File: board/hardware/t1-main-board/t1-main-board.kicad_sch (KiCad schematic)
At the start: 0 parts

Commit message: Board: capture blk.current-monitors
Five INA236 on I2C1 (0x40-0x43, 0x48) with their shunts, per power tree
§4.12 and BOM v1 lines 54 and 136. The measured branches are rails of
their own (VSYS_SRC, VSYS_LV_AUDIO, VSYS_AUDIO, VSYS_LV_BL, VSYS_P5V1),
fed through the shunts on this sheet; the charger, audio, backlight and
5.1 V sheets take them. The root's layout may leave a stack level empty,
so the block sits under the notes; IC bboxes hold turned rail values;
passive rows hold a bottom rail's text.

Co-Authored-By: Claude Opus 5.5 <noreply@anthropic.com>
Claude-Session: https://claude.ai/code/session_01Ei262h3TpgY9vyfNLMi5Mn
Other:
- added sheet Current monitors (current-monitors.kicad_sch)
- note added: "SoC, memory and the coprocessor; audio, from the DACs to the jacks; instrumentation"
- note removed: "SoC, memory and the coprocessor; audio, from the DACs to the jacks"

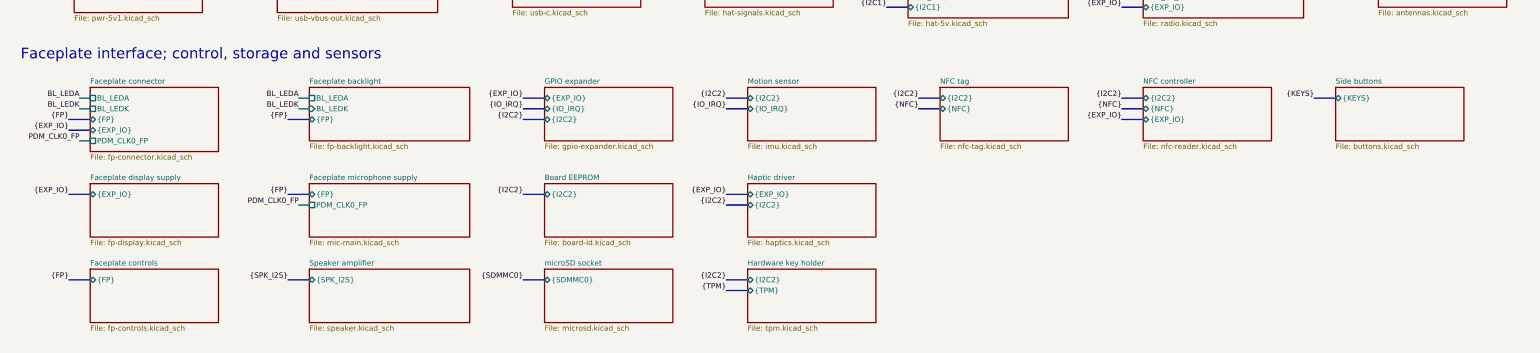
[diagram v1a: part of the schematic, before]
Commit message: Board: capture blk.status-led
LP5521 at 0x32 on I2C2 (BOM v1 line 105) with its charge-pump
capacitors, EN on vcca1v8_pmu, VDD from VSYS_LV through link #22;
LED_R/G/B reach the faceplate connector as the LED bus alias. The
faceplate row of the root is re-packed so five full columns sit left of
the title block.

Co-Authored-By: Claude Opus 5.5 <noreply@anthropic.com>
Claude-Session: https://claude.ai/code/session_01Ei262h3TpgY9vyfNLMi5Mn
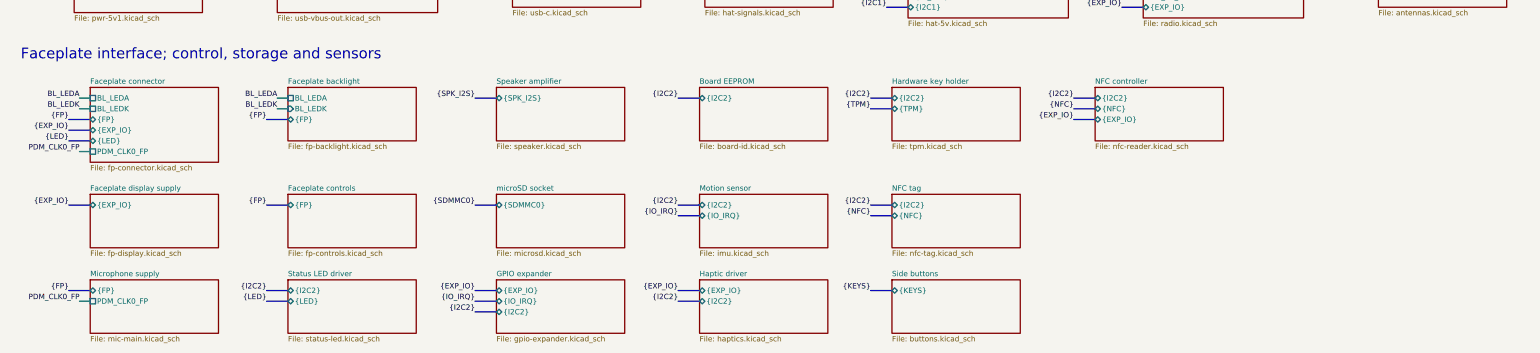
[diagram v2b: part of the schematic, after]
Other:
- sheet Faceplate microphone supply renamed Microphone supply
- added sheet Status LED driver (status-led.kicad_sch)
- sheet Faceplate connector ports: added {LED}; removed none

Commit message: Board: capture blk.debug
Debug UART2 (1.8 V) and I2S/DSD pads with ground pads, reset, PMIC and
power-key pads (PCB-T-09), a pad on every spare SoC GPIO whose pinout v1
row names one (the DEBUG bus, on the SoC's right edge), and a rail pad
for each power-tree rail no other sheet probes (PCB-T-02). Each DAC
sheet carries a pad on its MCLK. The spares pinout v1 leaves without a
pad now carry no-connect flags. On the root, facing sheet pins are
joined directly only where the route meets no other symbol.

Co-Authored-By: Claude Opus 5.5 <noreply@anthropic.com>
Claude-Session: https://claude.ai/code/session_01Ei262h3TpgY9vyfNLMi5Mn
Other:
- added sheet Test and debug access (debug.kicad_sch)
- sheet SoC ports: added {DEBUG}; removed none

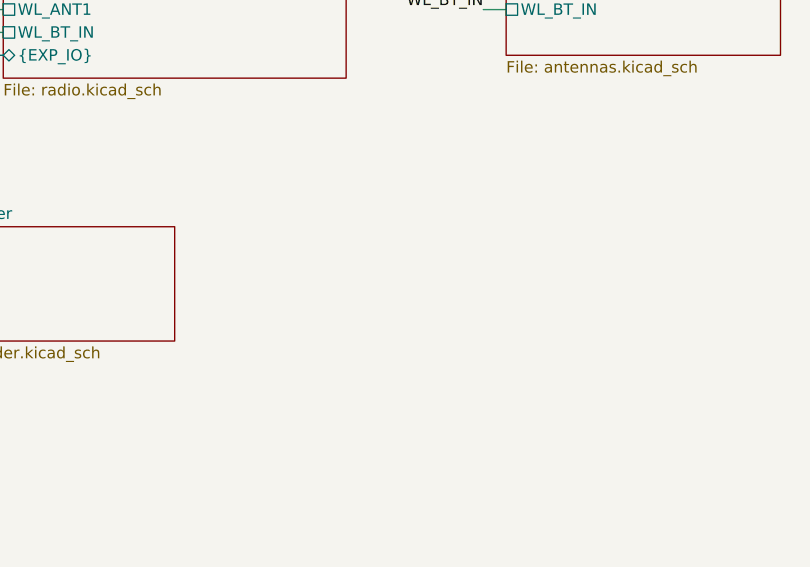
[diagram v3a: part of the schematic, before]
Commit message: Board: capture blk.cover-detect
COVER_DET_N on GPIO0_A6 (AJ38, PMUIO1, wake-capable), recorded in
pinout v1 (closes feature blocks G22): board-edge input and ground pads
for the case's actuator, 100 kΩ to vcc3v3_pmu, TPD1E10B06 at the pad
(BOM v1 line 143, PCB-L-10). The line rides the KEYS bus with the
buttons.

Co-Authored-By: Claude Opus 5.5 <noreply@anthropic.com>
Claude-Session: https://claude.ai/code/session_01Ei262h3TpgY9vyfNLMi5Mn
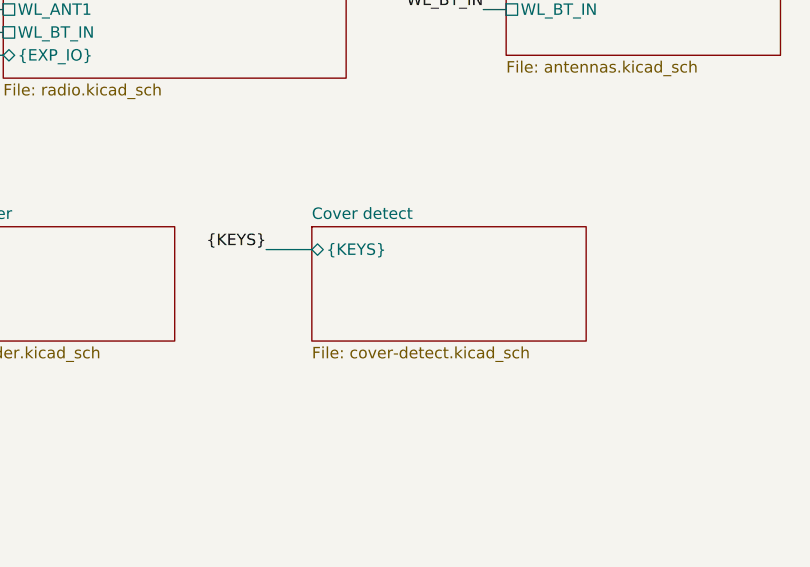
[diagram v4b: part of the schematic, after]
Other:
- added sheet Cover detect (cover-detect.kicad_sch)
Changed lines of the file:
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@@
   (property "Block" "blk.fp-display" (at 41.91 254.588 0) (effects (font (size 1.27 1.27)) (justify left top)) (hide yes))
   (pin "{EXP_IO}" bidirectional (at 41.91 241.3 180) (effects (font (size 1.27 1.27)) (justify left)))
-  (instances (project "t1-main-board" (path "/7746052e-d7f9-59ad-ba73-bd2b74439529" (page "57"))))
+  (instances (project "t1-main-board" (path "/7746052e-d7f9-59ad-ba73-bd2b74439529" (page "58"))))
 )
 (sheet (at 88.9 213.36) (size 30.48 12.7) (exclude_from_sim no) (in_bom yes) (on_board yes) (dnp no) (fields_autoplaced yes) (stroke (width 0.1524) (type solid)) (fill (color 0 0 0 0.0000))
@@
   (property "Block" "blk.fp-controls" (at 88.9 254.588 0) (effects (font (size 1.27 1.27)) (justify left top)) (hide yes))
   (pin "{FP}" bidirectional (at 88.9 241.3 180) (effects (font (size 1.27 1.27)) (justify left)))
-  (instances (project "t1-main-board" (path "/7746052e-d7f9-59ad-ba73-bd2b74439529" (page "58"))))
+  (instances (project "t1-main-board" (path "/7746052e-d7f9-59ad-ba73-bd2b74439529" (page "59"))))
 )
 (sheet (at 41.91 259.08) (size 30.48 12.7) (exclude_from_sim no) (in_bom yes) (on_board yes) (dnp no) (fields_autoplaced yes) (stroke (width 0.1524) (type solid)) (fill (color 0 0 0 0.0000))
@@
   (pin "{FP}" bidirectional (at 41.91 261.62 180) (effects (font (size 1.27 1.27)) (justify left)))
   (pin "PDM_CLK0_FP" passive (at 41.91 264.16 180) (effects (font (size 1.27 1.27)) (justify left)))
-  (instances (project "t1-main-board" (path "/7746052e-d7f9-59ad-ba73-bd2b74439529" (page "62"))))
+  (instances (project "t1-main-board" (path "/7746052e-d7f9-59ad-ba73-bd2b74439529" (page "63"))))
 )
 (sheet (at 138.43 259.08) (size 30.48 12.7) (exclude_from_sim no) (in_bom yes) (on_board yes) (dnp no) (fields_autoplaced yes) (stroke (width 0.1524) (type solid)) (fill (color 0 0 0 0.0000))
@@
   (pin "{IO_IRQ}" bidirectional (at 138.43 264.16 180) (effects (font (size 1.27 1.27)) (justify left)))
   (pin "{I2C2}" bidirectional (at 138.43 266.7 180) (effects (font (size 1.27 1.27)) (justify left)))
-  (instances (project "t1-main-board" (path "/7746052e-d7f9-59ad-ba73-bd2b74439529" (page "64"))))
+  (instances (project "t1-main-board" (path "/7746052e-d7f9-59ad-ba73-bd2b74439529" (page "65"))))
 )
 (sheet (at 186.69 213.36) (size 30.48 12.7) (exclude_from_sim no) (in_bom yes) (on_board yes) (dnp no) (fields_autoplaced yes) (stroke (width 0.1524) (type solid)) (fill (color 0 0 0 0.0000))
@@
   (property "Block" "blk.microsd" (at 138.43 254.588 0) (effects (font (size 1.27 1.27)) (justify left top)) (hide yes))
   (pin "{SDMMC0}" bidirectional (at 138.43 241.3 180) (effects (font (size 1.27 1.27)) (justify left)))
-  (instances (project "t1-main-board" (path "/7746052e-d7f9-59ad-ba73-bd2b74439529" (page "59"))))
+  (instances (project "t1-main-board" (path "/7746052e-d7f9-59ad-ba73-bd2b74439529" (page "60"))))
 )
 (sheet (at 186.69 238.76) (size 30.48 12.7) (exclude_from_sim no) (in_bom yes) (on_board yes) (dnp no) (fields_autoplaced yes) (stroke (width 0.1524) (type solid)) (fill (color 0 0 0 0.0000))
@@
   (pin "{I2C2}" bidirectional (at 186.69 241.3 180) (effects (font (size 1.27 1.27)) (justify left)))
   (pin "{IO_IRQ}" bidirectional (at 186.69 243.84 180) (effects (font (size 1.27 1.27)) (justify left)))
-  (instances (project "t1-main-board" (path "/7746052e-d7f9-59ad-ba73-bd2b74439529" (page "60"))))
+  (instances (project "t1-main-board" (path "/7746052e-d7f9-59ad-ba73-bd2b74439529" (page "61"))))
 )
 (sheet (at 138.43 213.36) (size 30.48 12.7) (exclude_from_sim no) (in_bom yes) (on_board yes) (dnp no) (fields_autoplaced yes) (stroke (width 0.1524) (type solid)) (fill (color 0 0 0 0.0000))
@@
   (pin "{EXP_IO}" bidirectional (at 186.69 261.62 180) (effects (font (size 1.27 1.27)) (justify left)))
   (pin "{I2C2}" bidirectional (at 186.69 264.16 180) (effects (font (size 1.27 1.27)) (justify left)))
-  (instances (project "t1-main-board" (path "/7746052e-d7f9-59ad-ba73-bd2b74439529" (page "65"))))
+  (instances (project "t1-main-board" (path "/7746052e-d7f9-59ad-ba73-bd2b74439529" (page "66"))))
 )
 (sheet (at 232.41 213.36) (size 30.48 12.7) (exclude_from_sim no) (in_bom yes) (on_board yes) (dnp no) (fields_autoplaced yes) (stroke (width 0.1524) (type solid)) (fill (color 0 0 0 0.0000))
@@
   (pin "{I2C2}" bidirectional (at 232.41 241.3 180) (effects (font (size 1.27 1.27)) (justify left)))
   (pin "{NFC}" bidirectional (at 232.41 243.84 180) (effects (font (size 1.27 1.27)) (justify left)))
-  (instances (project "t1-main-board" (path "/7746052e-d7f9-59ad-ba73-bd2b74439529" (page "61"))))
+  (instances (project "t1-main-board" (path "/7746052e-d7f9-59ad-ba73-bd2b74439529" (page "62"))))
 )
 (sheet (at 280.67 213.36) (size 30.48 12.7) (exclude_from_sim no) (in_bom yes) (on_board yes) (dnp no) (fields_autoplaced yes) (stroke (width 0.1524) (type solid)) (fill (color 0 0 0 0.0000))
@@
   (property "Block" "blk.buttons" (at 232.41 274.908 0) (effects (font (size 1.27 1.27)) (justify left top)) (hide yes))
   (pin "{KEYS}" bidirectional (at 232.41 261.62 180) (effects (font (size 1.27 1.27)) (justify left)))
-  (instances (project "t1-main-board" (path "/7746052e-d7f9-59ad-ba73-bd2b74439529" (page "66"))))
+  (instances (project "t1-main-board" (path "/7746052e-d7f9-59ad-ba73-bd2b74439529" (page "67"))))
 )
 (sheet (at 265.43 106.68) (size 30.48 12.7) (exclude_from_sim no) (in_bom yes) (on_board yes) (dnp no) (fields_autoplaced yes) (stroke (width 0.1524) (type solid)) (fill (color 0 0 0 0.0000))
@@
   (pin "{I2C2}" bidirectional (at 88.9 261.62 180) (effects (font (size 1.27 1.27)) (justify left)))
   (pin "{LED}" bidirectional (at 88.9 264.16 180) (effects (font (size 1.27 1.27)) (justify left)))
-  (instances (project "t1-main-board" (path "/7746052e-d7f9-59ad-ba73-bd2b74439529" (page "63"))))
+  (instances (project "t1-main-board" (path "/7746052e-d7f9-59ad-ba73-bd2b74439529" (page "64"))))
 )
 (sheet (at 363.22 132.08) (size 30.48 12.7) (exclude_from_sim no) (in_bom yes) (on_board yes) (dnp no) (fields_autoplaced yes) (stroke (width 0.1524) (type solid)) (fill (color 0 0 0 0.0000))
@@
   (pin "{KEYS}" bidirectional (at 363.22 142.24 180) (effects (font (size 1.27 1.27)) (justify left)))
   (instances (project "t1-main-board" (path "/7746052e-d7f9-59ad-ba73-bd2b74439529" (page "41"))))
+)
+(sheet (at 326.39 213.36) (size 30.48 12.7) (exclude_from_sim no) (in_bom yes) (on_board yes) (dnp no) (fields_autoplaced yes) (stroke (width 0.1524) (type solid)) (fill (color 0 0 0 0.0000))
+  (property "Sheetname" "Cover detect" (at 326.39 212.648 0) (effects (font (size 1.27 1.27)) (justify left bottom)))
+  (property "Sheetfile" "cover-detect.kicad_sch" (at 326.39 226.648 0) (effects (font (size 1.27 1.27)) (justify left top)))
+  (property "Block" "blk.cover-detect" (at 326.39 229.188 0) (effects (font (size 1.27 1.27)) (justify left top)) (hide yes))
+  (pin "{KEYS}" bidirectional (at 326.39 215.9 180) (effects (font (size 1.27 1.27)) (justify left)))
+  (instances (project "t1-main-board" (path "/7746052e-d7f9-59ad-ba73-bd2b74439529" (page "57"))))
 )
 (wire (pts (xy 109.22 53.34) (xy 106.68 53.34)) (stroke (width 0) (type default)))
@@
 (bus (pts (xy 363.22 142.24) (xy 358.14 142.24)) (stroke (width 0) (type default)))
 (label "{KEYS}" (at 358.14 142.24 180) (effects (font (size 1.27 1.27)) (justify right bottom)))
+(bus (pts (xy 326.39 215.9) (xy 321.31 215.9)) (stroke (width 0) (type default)))
+(label "{KEYS}" (at 321.31 215.9 180) (effects (font (size 1.27 1.27)) (justify right bottom)))
 (wire (pts (xy 293.37 50.8) (xy 293.37 48.26)) (stroke (width 0) (type default)))
 (label "VCC_DDR_SRC" (at 293.37 48.26 90) (effects (font (size 1.27 1.27)) (justify left bottom)))

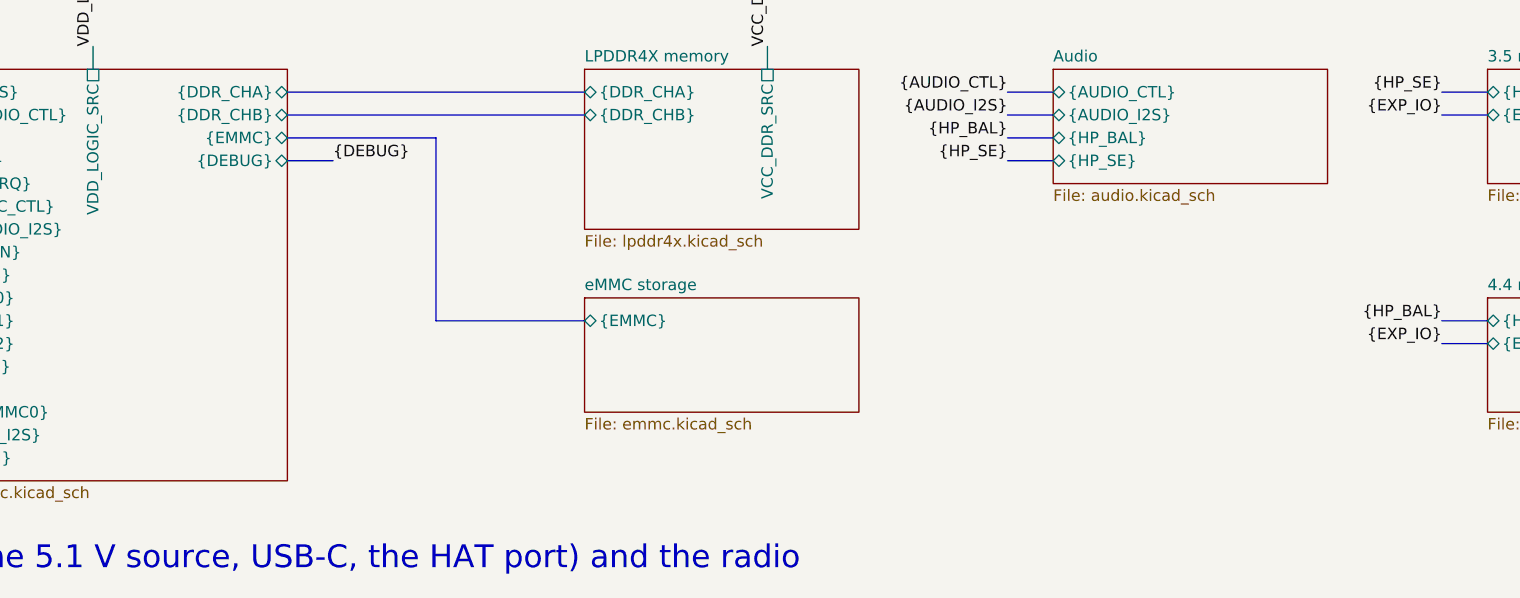
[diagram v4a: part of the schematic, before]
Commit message: Board: capture blk.mic-ambient and links #34, #35
IM73D122 on PDM CLK1 and SDI1 (BOM v1 line 34, pinout v1 AK2 and 1P2),
LR to ground, 22 Ω clock series, VDD from MIC_1V8 through link #35.
Link #34 on blk.mic-main makes the faceplate branch the rail MIC_1V8_FP
for contact 40 (power tree §4.12, G10). kicad-lib moves to e46bda4 for
the IM73D122, TPS3808G01, SN74LVC1G58 and BAT54 parts.

Co-Authored-By: Claude Opus 5.5 <noreply@anthropic.com>
Claude-Session: https://claude.ai/code/session_01Ei262h3TpgY9vyfNLMi5Mn
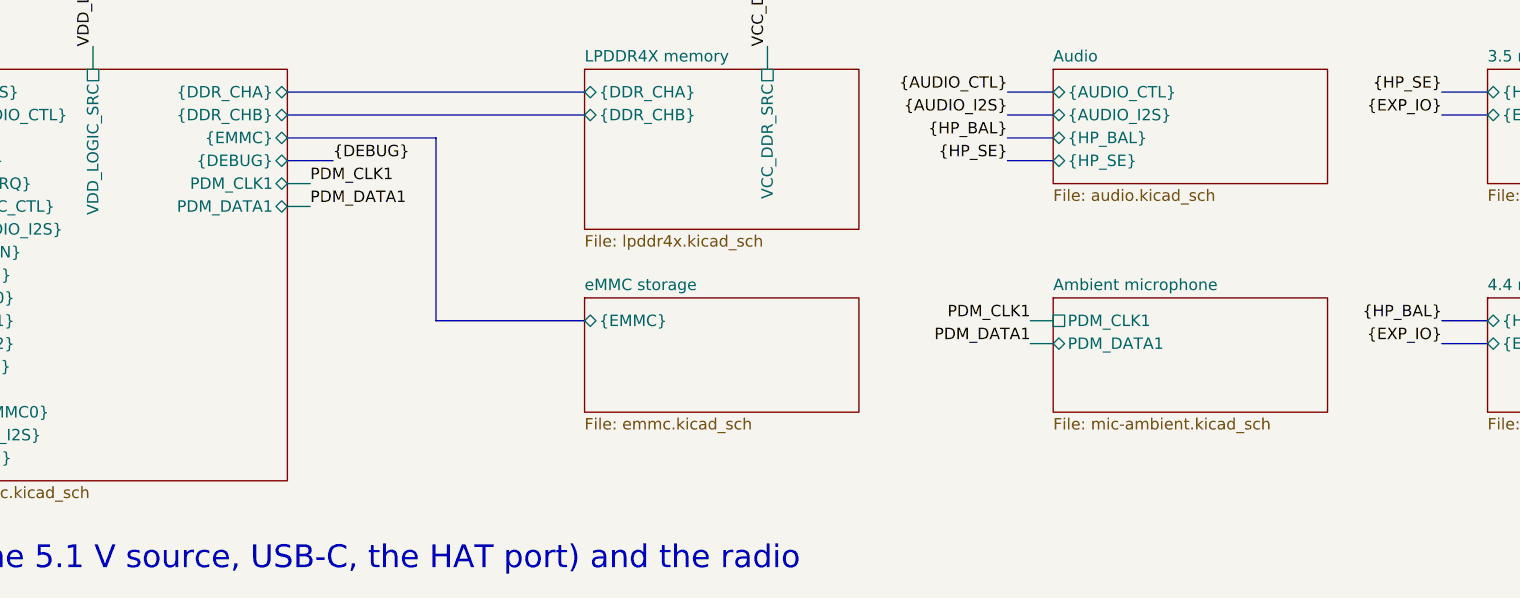
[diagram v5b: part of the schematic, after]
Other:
- added sheet Ambient microphone (mic-ambient.kicad_sch)
- sheet SoC ports: added PDM_CLK1, PDM_DATA1; removed none

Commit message: Board: capture blk.maskrom
Power + Vol- at a cold power-on pull eMMC D0 low inside the TPS3808G01
boot window (BOM v1 lines 35, 78, 97, 98; sim/maskrom): SENSE 280k/100k,
CT 390 nF, WINDOW_N with its pad, SN74LVC1G57 and SN74LVC1G58 on
vcca1v8_pmu, BAT54 from PWRON_N, DMG1012T through 1 kΩ to EMMC_D0.
Every block in use now has its sheet; the README states the remaining
single-pin nets.

Co-Authored-By: Claude Opus 5.5 <noreply@anthropic.com>
Claude-Session: https://claude.ai/code/session_01Ei262h3TpgY9vyfNLMi5Mn
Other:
- added sheet MaskROM entry (maskrom.kicad_sch)
- note added: "SoC, memory, the coprocessor and MaskROM entry; audio, from the DACs to the jacks; instrumentation and debug"
- note removed: "SoC, memory and the coprocessor; audio, from the DACs to the jacks; instrumentation"
